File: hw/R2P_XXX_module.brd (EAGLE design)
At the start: 40 x 40 mm, 32 parts, among them U1 STM32F103CX, U5 LD3985XX, X1 MICROMATCH-6

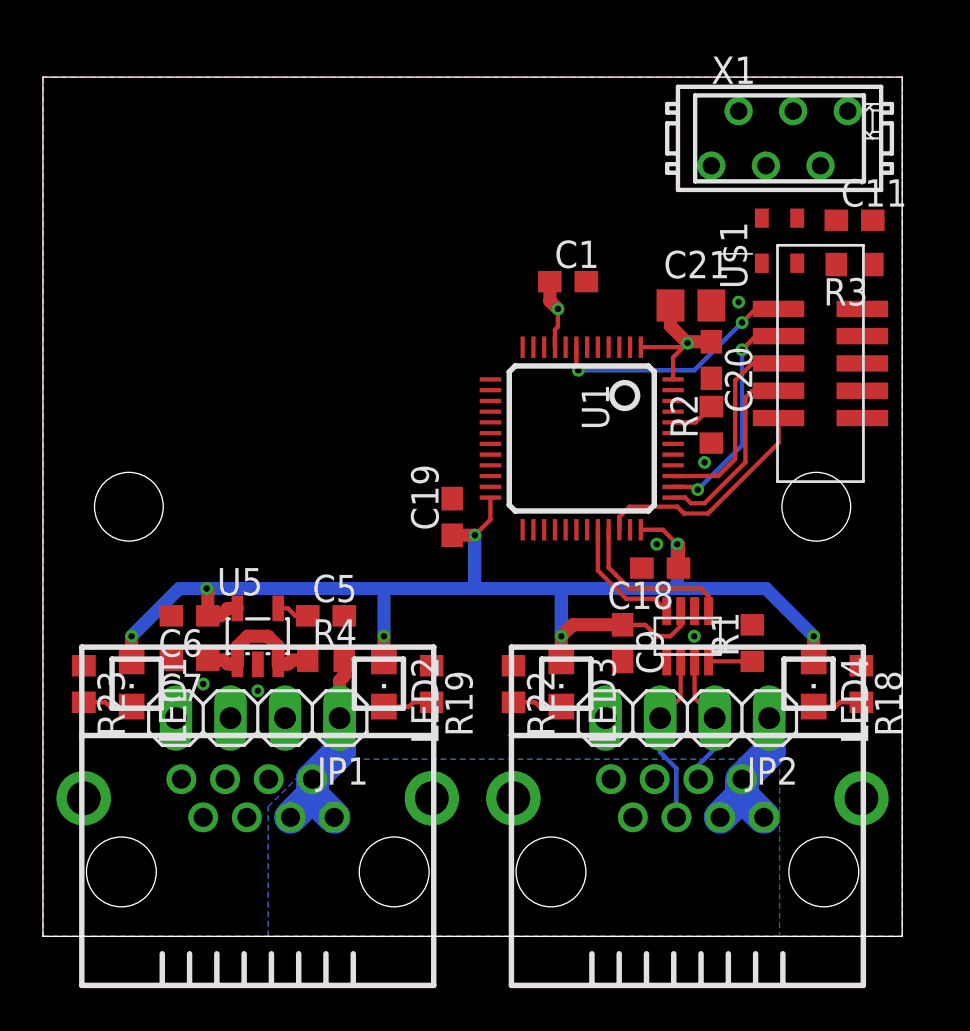
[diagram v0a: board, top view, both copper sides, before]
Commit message: Board layout completed
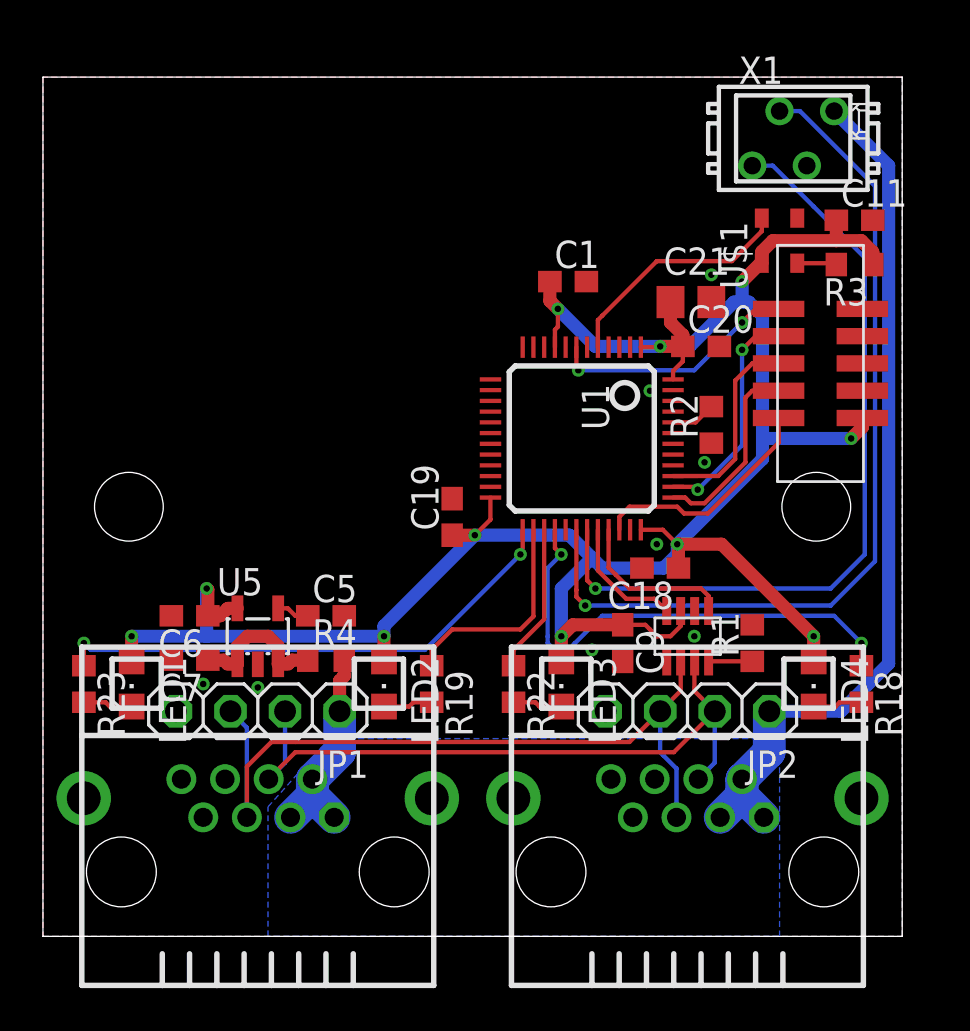
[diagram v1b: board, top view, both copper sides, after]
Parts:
- JP1, JP2: device pinhead:1X04 -> misc:1X04
- X1: value MICROMATCH-6 -> MICROMATCH-4; device con-amp-micromatch:MICROMATCH-6 -> con-amp-micromatch:MICROMATCH-4
- moved C20 0.79 mm to (30.6, 27.5), turned to 0 degrees
- moved X1 0.63 mm to (34.9, 37.1)
- moved JP2 0.32 mm to (30.0, 10.5)
- moved JP1 0.32 mm to (10.0, 10.5)
- moved C21 0.16 mm to (30.2, 29.5)
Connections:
- net UART_RX: now also X1.4
- net UART_TX: now also X1.3
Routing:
- net UART_TX: track 0.00 -> 41.4 mm, vias 0 -> 1
- net +3V3: track 74.2 -> 112.4 mm, vias 9 -> 11
- net UART_RX: track 0.00 -> 36.9 mm, vias 0 -> 1
- net +5V: track 18.3 -> 51.9 mm
- net CANL: track 7.97 -> 35.9 mm
- net CANH: track 6.18 -> 31.7 mm
- net LED1: track 0.00 -> 24.5 mm, vias 0 -> 2
- net LED4: track 0.00 -> 22.6 mm, vias 0 -> 2
- net OSC_IN: track 0.00 -> 11.2 mm
- net LED2: track 0.00 -> 10.2 mm
- net LED3: track 0.00 -> 6.92 mm
- net N$3: track 0.00 -> 1.84 mm

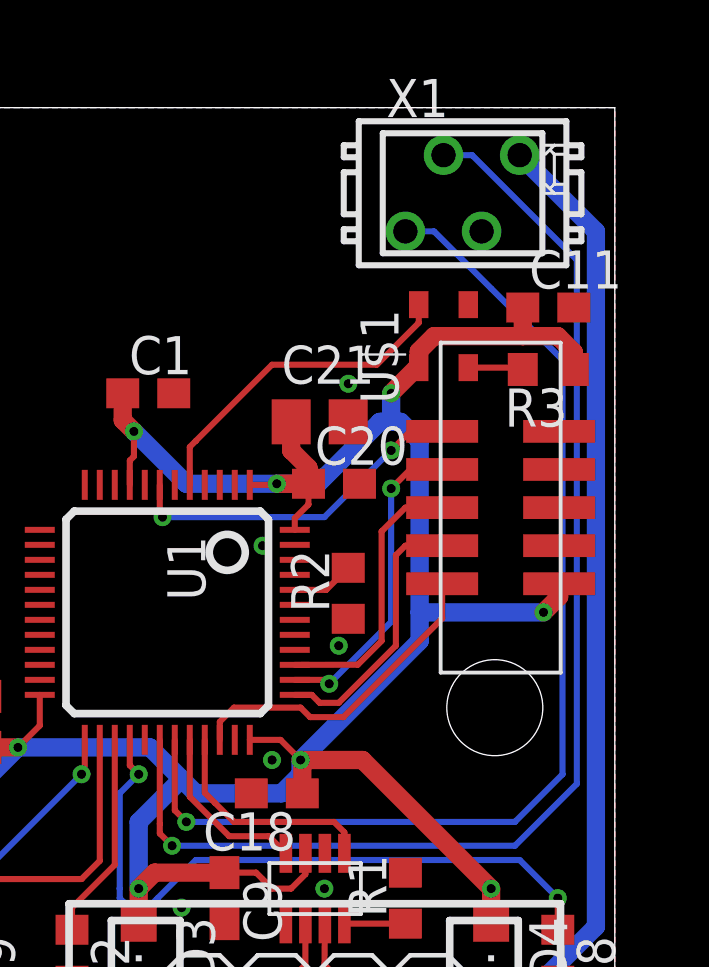
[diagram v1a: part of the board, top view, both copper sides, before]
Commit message: Updated micromatch connector
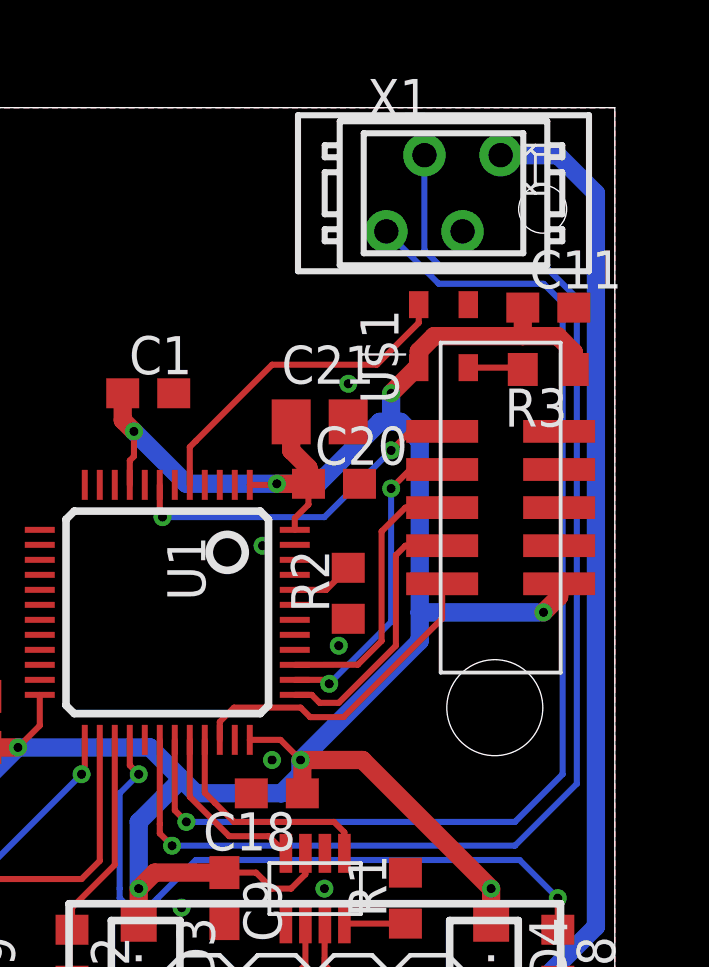
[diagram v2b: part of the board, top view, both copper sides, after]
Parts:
- X1: device con-amp-micromatch:MICROMATCH-4 -> tyco:MICROMATCH-4
- moved X1 0.63 mm to (34.3, 37.1)
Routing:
- net UART_RX: track 36.9 -> 38.7 mm
- net UART_TX: track 41.4 -> 43.2 mm
- net +5V: track 51.9 -> 53.3 mm
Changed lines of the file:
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@@
 <grid distance="0.0125" unitdist="inch" unit="inch" style="lines" multiple="1" display="no" altdistance="0.00625" altunitdist="inch" altunit="inch"/>
 <layers>
-<layer number="1" name="Top" color="4" fill="1" visible="yes" active="yes"/>
-<layer number="16" name="Bottom" color="1" fill="1" visible="no" active="yes"/>
+<layer number="1" name="Top" color="4" fill="1" visible="no" active="yes"/>
+<layer number="16" name="Bottom" color="1" fill="1" visible="yes" active="yes"/>
 <layer number="17" name="Pads" color="2" fill="1" visible="yes" active="yes"/>
 <layer number="18" name="Vias" color="2" fill="1" visible="yes" active="yes"/>
 <layer number="19" name="Unrouted" color="6" fill="1" visible="yes" active="yes"/>
 <layer number="20" name="Dimension" color="15" fill="1" visible="yes" active="yes"/>
-<layer number="21" name="tPlace" color="7" fill="1" visible="yes" active="yes"/>
-<layer number="22" name="bPlace" color="7" fill="1" visible="no" active="yes"/>
-<layer number="23" name="tOrigins" color="15" fill="1" visible="yes" active="yes"/>
-<layer number="24" name="bOrigins" color="15" fill="1" visible="no" active="yes"/>
+<layer number="21" name="tPlace" color="7" fill="1" visible="no" active="yes"/>
+<layer number="22" name="bPlace" color="7" fill="1" visible="yes" active="yes"/>
+<layer number="23" name="tOrigins" color="15" fill="1" visible="no" active="yes"/>
+<layer number="24" name="bOrigins" color="15" fill="1" visible="yes" active="yes"/>
 <layer number="25" name="tNames" color="7" fill="1" visible="no" active="yes"/>
 <layer number="26" name="bNames" color="7" fill="1" visible="no" active="yes"/>
@@
 <layer number="35" name="tGlue" color="7" fill="4" visible="no" active="yes"/>
 <layer number="36" name="bGlue" color="7" fill="5" visible="no" active="yes"/>
-<layer number="37" name="tTest" color="7" fill="1" visible="yes" active="yes"/>
-<layer number="38" name="bTest" color="7" fill="1" visible="no" active="yes"/>
-<layer number="39" name="tKeepout" color="4" fill="11" visible="yes" active="yes"/>
-<layer number="40" name="bKeepout" color="1" fill="11" visible="no" active="yes"/>
-<layer number="41" name="tRestrict" color="4" fill="10" visible="yes" active="yes"/>
-<layer number="42" name="bRestrict" color="1" fill="10" visible="no" active="yes"/>
+<layer number="37" name="tTest" color="7" fill="1" visible="no" active="yes"/>
+<layer number="38" name="bTest" color="7" fill="1" visible="yes" active="yes"/>
+<layer number="39" name="tKeepout" color="4" fill="11" visible="no" active="yes"/>
+<layer number="40" name="bKeepout" color="1" fill="11" visible="yes" active="yes"/>
+<layer number="41" name="tRestrict" color="4" fill="10" visible="no" active="yes"/>
+<layer number="42" name="bRestrict" color="1" fill="10" visible="yes" active="yes"/>
 <layer number="43" name="vRestrict" color="2" fill="10" visible="yes" active="yes"/>
 <layer number="44" name="Drills" color="7" fill="1" visible="yes" active="yes"/>
@@
 <layer number="49" name="Reference" color="7" fill="1" visible="yes" active="yes"/>
 <layer number="50" name="dxf" color="7" fill="1" visible="no" active="no"/>
-<layer number="51" name="tDocu" color="7" fill="1" visible="yes" active="yes"/>
-<layer number="52" name="bDocu" color="7" fill="1" visible="no" active="yes"/>
+<layer number="51" name="tDocu" color="7" fill="1" visible="no" active="yes"/>
+<layer number="52" name="bDocu" color="7" fill="1" visible="yes" active="yes"/>
 <layer number="53" name="tGND_GNDA" color="7" fill="9" visible="no" active="no"/>
 <layer number="54" name="bGND_GNDA" color="1" fill="9" visible="no" active="no"/>
@@
 <element name="R4" library="rcl" package="R0603" value="PTC" x="13.17625" y="12.85875"/>
 <element name="C1" library="rcl" package="C0603" value="100n" x="24.4475" y="30.48"/>
-<element name="X1" library="con-amp-micromatch" package="MICROMATCH-4" value="MICROMATCH-4" x="34.925" y="37.1475">
-<attribute name="OC_NEWARK" value="19R8124" x="34.925" y="37.1475" size="1.778" layer="27" display="off"/>
-<attribute name="MPN" value="7-215464-4" x="34.925" y="37.1475" size="1.778" layer="27" display="off"/>
-<attribute name="MF" value="" x="34.925" y="37.1475" size="1.778" layer="27" display="off"/>
-<attribute name="OC_FARNELL" value="3784629" x="34.925" y="37.1475" size="1.778" layer="27" display="off"/>
-</element>
+<element name="X1" library="tyco" package="MICROMATCH-4" value="MICROMATCH-4" x="34.29" y="37.1475"/>
 </elements>
 <signals>
@@
 <wire x1="25.24125" y1="15.39875" x2="36.67125" y2="15.39875" width="0.2032" layer="16"/>
 <wire x1="36.67125" y1="15.39875" x2="38.735" y2="17.4625" width="0.2032" layer="16"/>
-<wire x1="38.735" y1="17.4625" x2="38.735" y2="34.925" width="0.2032" layer="16"/>
-<wire x1="38.735" y1="34.925" x2="35.2425" y2="38.4175" width="0.2032" layer="16"/>
-<wire x1="35.2425" y1="38.4175" x2="34.29" y2="38.4175" width="0.2032" layer="16"/>
+<wire x1="38.735" y1="17.4625" x2="38.735" y2="33.655" width="0.2032" layer="16"/>
 <wire x1="24.8325" y1="15.8075" x2="25.24125" y2="15.39875" width="0.2032" layer="1"/>
+<wire x1="33.655" y1="38.4175" x2="33.655" y2="35.2425" width="0.2032" layer="16"/>
+<wire x1="33.655" y1="35.2425" x2="34.29" y2="34.6075" width="0.2032" layer="16"/>
+<wire x1="34.29" y1="34.6075" x2="37.7825" y2="34.6075" width="0.2032" layer="16"/>
+<wire x1="37.7825" y1="34.6075" x2="38.735" y2="33.655" width="0.2032" layer="16"/>
 </signal>
 <signal name="UART_RX">
@@
 <wire x1="36.67125" y1="16.1925" x2="38.25875" y2="17.78" width="0.2032" layer="16"/>
 <wire x1="38.25875" y1="17.78" x2="38.25875" y2="31.59125" width="0.2032" layer="16"/>
-<wire x1="38.25875" y1="31.59125" x2="35.8775" y2="33.9725" width="0.2032" layer="16"/>
 <wire x1="25.3325" y1="18.9275" x2="25.3325" y2="16.5775" width="0.2032" layer="1"/>
 <wire x1="25.3325" y1="16.5775" x2="25.7175" y2="16.1925" width="0.2032" layer="1"/>
-<wire x1="35.8775" y1="33.9725" x2="33.9725" y2="35.8775" width="0.2032" layer="16"/>
-<wire x1="33.9725" y1="35.8775" x2="33.02" y2="35.8775" width="0.2032" layer="16"/>
+<wire x1="32.385" y1="35.8775" x2="34.13125" y2="34.13125" width="0.2032" layer="16"/>
+<wire x1="34.13125" y1="34.13125" x2="37.62375" y2="34.13125" width="0.2032" layer="16"/>
+<wire x1="37.62375" y1="34.13125" x2="38.25875" y2="33.49625" width="0.2032" layer="16"/>
+<wire x1="38.25875" y1="33.49625" x2="38.25875" y2="31.59125" width="0.2032" layer="16"/>
 </signal>
 <signal name="CAN_RX">
@@
 <wire x1="37.1475" y1="10.4775" x2="39.37" y2="12.7" width="0.6096" layer="16"/>
 <wire x1="39.37" y1="12.7" x2="39.37" y2="35.8775" width="0.6096" layer="16"/>
-<wire x1="39.37" y1="35.8775" x2="36.83" y2="38.4175" width="0.6096" layer="16"/>
+<wire x1="36.195" y1="38.4175" x2="38.1" y2="38.4175" width="0.6096" layer="16"/>
+<wire x1="38.1" y1="38.4175" x2="39.37" y2="37.1475" width="0.6096" layer="16"/>
+<wire x1="39.37" y1="37.1475" x2="39.37" y2="35.8775" width="0.6096" layer="16"/>
 </signal>
 <signal name="N$5">

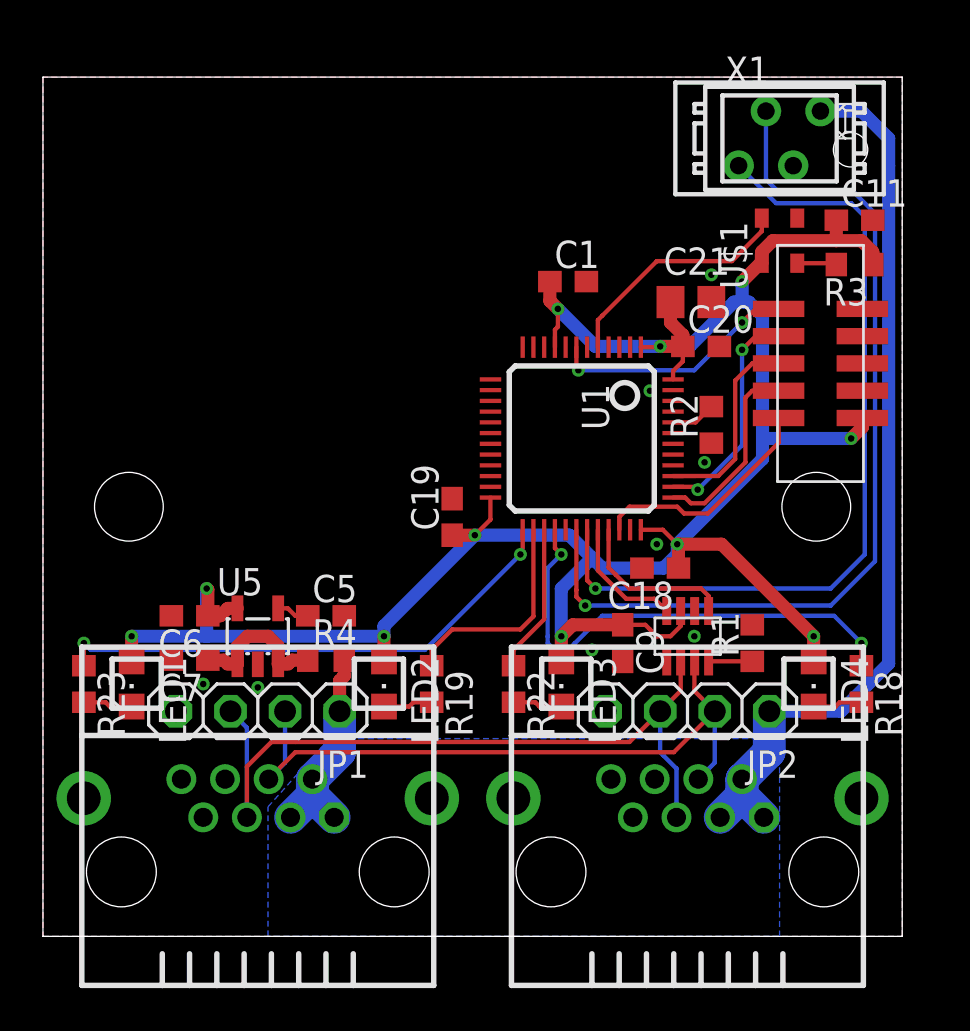
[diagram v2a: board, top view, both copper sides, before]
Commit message: Added space for UART connector
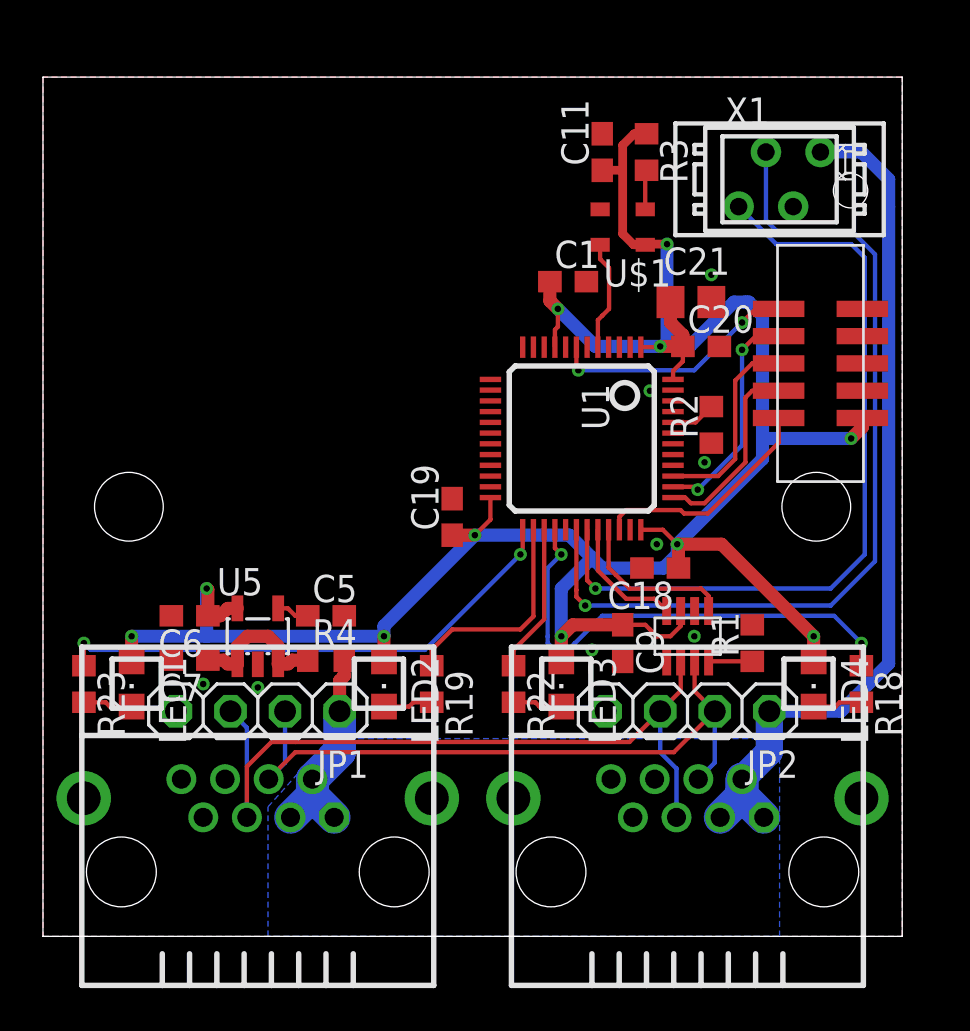
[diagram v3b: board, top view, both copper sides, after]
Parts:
- moved C11 12.2 mm to (26.0, 36.5), turned to 90 degrees
- moved R3 11.0 mm to (28.1, 36.5), turned to 270 degrees
- moved U$1 7.33 mm to (27.0, 33.0), turned to 180 degrees
- moved X1 1.91 mm to (34.3, 35.2)
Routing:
- net OSC_IN: track 11.2 -> 5.15 mm
- net +3V3: track 112.4 -> 116.2 mm
- net UART_RX: track 38.7 -> 36.8 mm
- net UART_TX: track 43.2 -> 41.2 mm
- net +5V: track 53.3 -> 51.4 mm
